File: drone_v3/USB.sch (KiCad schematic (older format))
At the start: 3 parts, among them J1 USB_B_Micro, U2 USBLC6-2SC6

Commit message: add alot
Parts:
- added D6: DIODE, Diode_SMD:D_0805_2012Metric_Pad1.15x1.40mm_HandSolder, symbol pspice:DIODE
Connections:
- net VCC is gone; now on net +5V: C28.1, U2.5 (VBUS)
- net +5V: now also D6.2 (A); no longer J1.1 (VBUS)
- new net: D6.1 (K), J1.1 (VBUS)
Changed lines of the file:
@@
 $EndComp
 NoConn ~ 3250 4000
-Wire Wire Line
-	3650 3400 3750 3400
 NoConn ~ 3650 3800
 Wire Wire Line
@@
 Wire Wire Line
 	3800 3700 3650 3700
-$Comp
-L power:+5V #PWR0104
-U 1 1 5F38D86C
-P 3750 3400
-F 0 "#PWR0104" H 3750 3250 50  0001 C CNN
-F 1 "+5V" H 3765 3573 50  0000 C CNN
-F 2 "" H 3750 3400 50  0001 C CNN
-F 3 "" H 3750 3400 50  0001 C CNN
-	1    3750 3400
-	0    1    1    0
-$EndComp
 Text Label 3750 3600 2    50   ~ 0
 D+
@@
 	1    0    0    -1
 $EndComp
-$Comp
-L power:VCC #PWR0106
-U 1 1 5F29A1DC
-P 5100 2850
-F 0 "#PWR0106" H 5100 2700 50  0001 C CNN
-F 1 "VCC" H 5115 3023 50  0000 C CNN
-F 2 "" H 5100 2850 50  0001 C CNN
-F 3 "" H 5100 2850 50  0001 C CNN
-	1    5100 2850
-	1    0    0    -1
-$EndComp
 Text GLabel 6450 3100 2    50   Input ~ 0
 USB_D+
@@
 	1    0    0    -1
 $EndComp
+$Comp
+L power:+5V #PWR0106
+U 1 1 5F3E2968
+P 5100 2850
+F 0 "#PWR0106" H 5100 2700 50  0001 C CNN
+F 1 "+5V" H 5115 3023 50  0000 C CNN
+F 2 "" H 5100 2850 50  0001 C CNN
+F 3 "" H 5100 2850 50  0001 C CNN
+	1    5100 2850
+	1    0    0    -1
+$EndComp
+Wire Wire Line
+	3650 3400 3750 3400
+$Comp
+L pspice:DIODE D?
+U 1 1 5F3E934F
+P 3950 3400
+AR Path="/5F3E934F" Ref="D?"  Part="1"
+AR Path="/5F569749/5F3E934F" Ref="D?"  Part="1"
+AR Path="/5F2F6324/5F3E934F" Ref="D6"  Part="1"
+F 0 "D6" V 3904 3528 50  0000 L CNN
+F 1 "DIODE" V 3995 3528 50  0000 L CNN
+F 2 "Diode_SMD:D_0805_2012Metric_Pad1.15x1.40mm_HandSolder" H 3950 3400 50  0001 C CNN
+F 3 "~" H 3950 3400 50  0001 C CNN
+	1    3950 3400
+	1    0    0    -1
+$EndComp
+$Comp
+L power:+5V #PWR0104
+U 1 1 5F38D86C
+P 4150 3300
+F 0 "#PWR0104" H 4150 3150 50  0001 C CNN
+F 1 "+5V" H 4165 3473 50  0000 C CNN
+F 2 "" H 4150 3300 50  0001 C CNN
+F 3 "" H 4150 3300 50  0001 C CNN
+	1    4150 3300
+	1    0    0    -1
+$EndComp
+Wire Wire Line
+	4150 3400 4150 3300
 $EndSCHEMATC

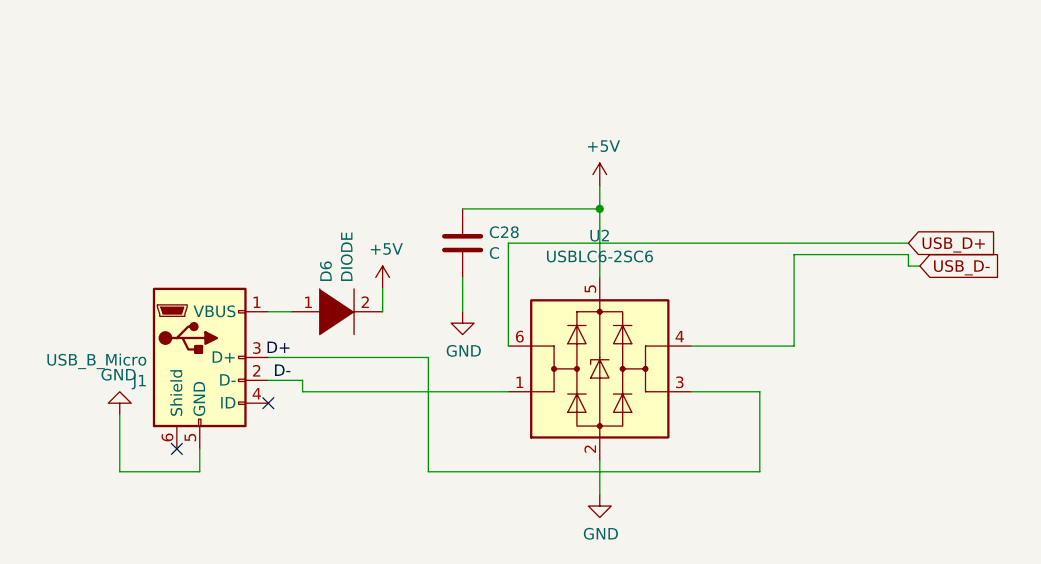
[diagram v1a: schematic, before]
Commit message: change 20602 to 20948, ms5611 to bmp180
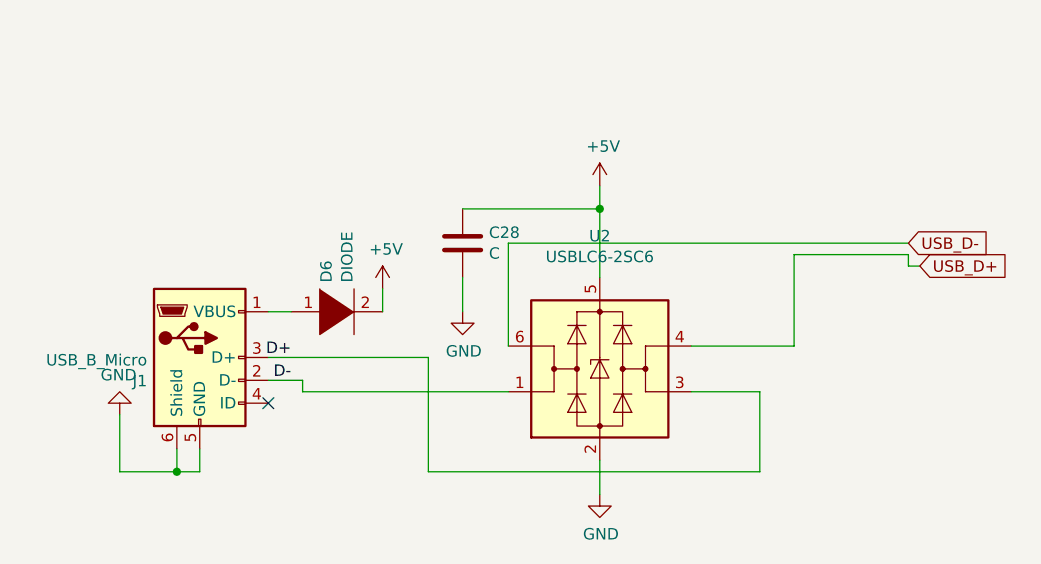
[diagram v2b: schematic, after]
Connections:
- net GND: now also J1.6 (Shield)
- net USB_D+: now also U2.4 (I/O2); no longer U2.6 (I/O1)
- net USB_D-: now also U2.6 (I/O1); no longer U2.4 (I/O2)
- no-connect marks 2 -> 1
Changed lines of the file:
@@
-	1    0    0    -1
-$EndComp
-$Comp
-L Connector:USB_B_Micro J1
-U 1 1 5F38D846
-P 3350 3600
-F 0 "J1" H 3120 3497 50  0000 R CNN
-F 1 "USB_B_Micro" H 3120 3588 50  0000 R CNN
-F 2 "Connector_USB:USB_Micro-B_Molex-105017-0001" H 3500 3550 50  0001 C CNN
-F 3 "~" H 3500 3550 50  0001 C CNN
-	1    3350 3600
 	1    0    0    -1
 $EndComp
@@
 	3350 4000 3350 4100
 Wire Wire Line
-	3350 4100 3000 4100
+	3350 4100 3250 4100
 Wire Wire Line
 	3000 4100 3000 3850
@@
 	-1   0    0    1
 $EndComp
-NoConn ~ 3250 4000
 NoConn ~ 3650 3800
 Wire Wire Line
@@
 	1    0    0    -1
 $EndComp
-Text GLabel 6450 3100 2    50   Input ~ 0
-USB_D+
-Text GLabel 6500 3200 2    50   Input ~ 0
-USB_D-
 Wire Wire Line
 	6500 3200 6450 3200
@@
 Wire Wire Line
 	4150 3400 4150 3300
+Text GLabel 6450 3100 2    50   Input ~ 0
+USB_D-
+Text GLabel 6500 3200 2    50   Input ~ 0
+USB_D+
+$Comp
+L Connector:USB_B_Micro J1
+U 1 1 5F38D846
+P 3350 3600
+F 0 "J1" H 3120 3497 50  0000 R CNN
+F 1 "USB_B_Micro" H 3120 3588 50  0000 R CNN
+F 2 "Connector_USB:USB_Micro-B_Molex-105017-0001" H 3500 3550 50  0001 C CNN
+F 3 "~" H 3500 3550 50  0001 C CNN
+	1    3350 3600
+	1    0    0    -1
+$EndComp
+Wire Wire Line
+	3250 4000 3250 4100
+Connection ~ 3250 4100
+Wire Wire Line
+	3250 4100 3000 4100
 $EndSCHEMATC

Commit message: add alot
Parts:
- D6: footprint Diode_SMD:D_0805_2012Metric_Pad1.15x1.40mm_HandSolder -> Diode_SMD:D_1206_3216Metric
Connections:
- net +5V: no longer D6.2 (A)
- new net PWR_IN: D6.2 (A)
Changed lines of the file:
@@
 F 0 "D6" V 3904 3528 50  0000 L CNN
 F 1 "DIODE" V 3995 3528 50  0000 L CNN
-F 2 "Diode_SMD:D_0805_2012Metric_Pad1.15x1.40mm_HandSolder" H 3950 3400 50  0001 C CNN
+F 2 "Diode_SMD:D_1206_3216Metric" H 3950 3400 50  0001 C CNN
 F 3 "~" H 3950 3400 50  0001 C CNN
 	1    3950 3400
 	1    0    0    -1
 $EndComp
-$Comp
-L power:+5V #PWR0104
-U 1 1 5F38D86C
-P 4150 3300
-F 0 "#PWR0104" H 4150 3150 50  0001 C CNN
-F 1 "+5V" H 4165 3473 50  0000 C CNN
-F 2 "" H 4150 3300 50  0001 C CNN
-F 3 "" H 4150 3300 50  0001 C CNN
-	1    4150 3300
-	1    0    0    -1
-$EndComp
-Wire Wire Line
-	4150 3400 4150 3300
 Text GLabel 6450 3100 2    50   Input ~ 0
 USB_D-
@@
 Wire Wire Line
 	3250 4100 3000 4100
+Text GLabel 4150 3000 1    50   Input ~ 0
+PWR_IN
+Wire Wire Line
+	4150 3000 4150 3400
 $EndSCHEMATC

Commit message: fix alot
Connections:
- net +5V is gone; now on net VBUS: C28.1, U2.5 (VBUS)
- net VBUS: now reaches D6.1 (K), J1.1 (VBUS)
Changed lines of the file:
@@
 Wire Wire Line
 	4500 2950 5100 2950
-Connection ~ 5100 2950
-Wire Wire Line
-	5100 2950 5100 2850
 Wire Wire Line
 	4500 3250 4500 3400
@@
 F 3 "" H 4500 3400 50  0001 C CNN
 	1    4500 3400
-	1    0    0    -1
-$EndComp
-$Comp
-L power:+5V #PWR0106
-U 1 1 5F3E2968
-P 5100 2850
-F 0 "#PWR0106" H 5100 2700 50  0001 C CNN
-F 1 "+5V" H 5115 3023 50  0000 C CNN
-F 2 "" H 5100 2850 50  0001 C CNN
-F 3 "" H 5100 2850 50  0001 C CNN
-	1    5100 2850
 	1    0    0    -1
 $EndComp
@@
 Wire Wire Line
 	4150 3000 4150 3400
+Wire Wire Line
+	3750 2900 3750 3400
+Text GLabel 3750 2900 1    50   Input ~ 0
+VBUS
+Wire Wire Line
+	5100 2450 5100 2950
+Text GLabel 5100 2450 1    50   Input ~ 0
+VBUS
 $EndSCHEMATC
